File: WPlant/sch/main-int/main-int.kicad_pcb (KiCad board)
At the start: 2 copper layers, 135 x 85 mm, 139 parts, among them J1 PROG/JTAG, J10 Ext, J11 HSensor, J12 HSensor, J13 HSensor, J14 HSensor, J15 HSensor, J16 HSensor, J17 HSensor, J18 WaterLevel, J5 220V, J6 Conn_01x08_Pin, J8 eInk-Buttons, J9 Leak, M1 Motor_DC, Q1 FDS9926A, Q2 FDS9926A, Q3 FDS9926A, Q4 FDS9926A, U1 SIWG917Y121MGABAR, U10 SP485EEN-L/TR, U11 TXU0102QDCURQ1, U12 CD74HCT4051M96, U13 CD74HCT4051M96, U14 SN74LVC1G14DBV, U3 AP64352SP-13, U4 AP64352SP-13, U5 TC4427AEOA713, U6 AP2204R-5.0, U7 74HC594, U8 NC7S02P5, U9 INA180A2, X1 SIT1552AI-JE-DCC-32.768D

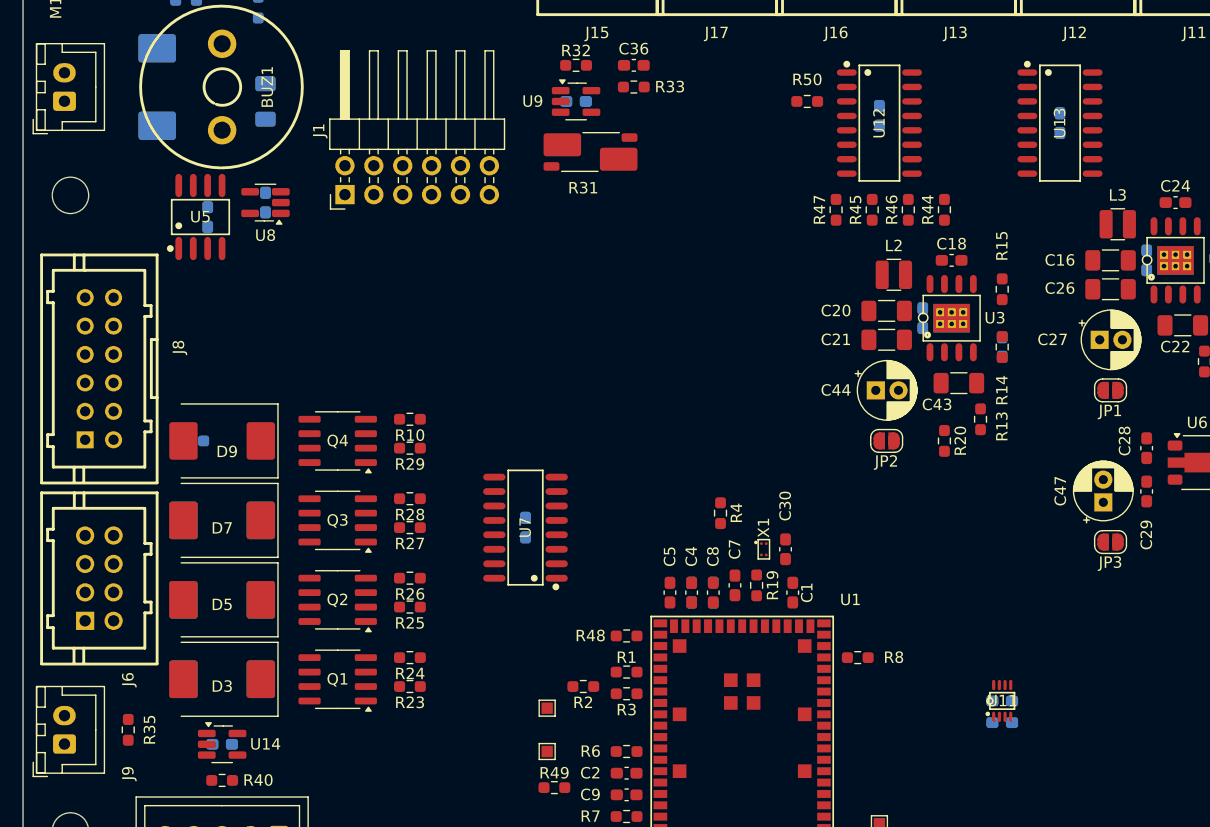
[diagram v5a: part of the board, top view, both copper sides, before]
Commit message: Started routing of MainInt
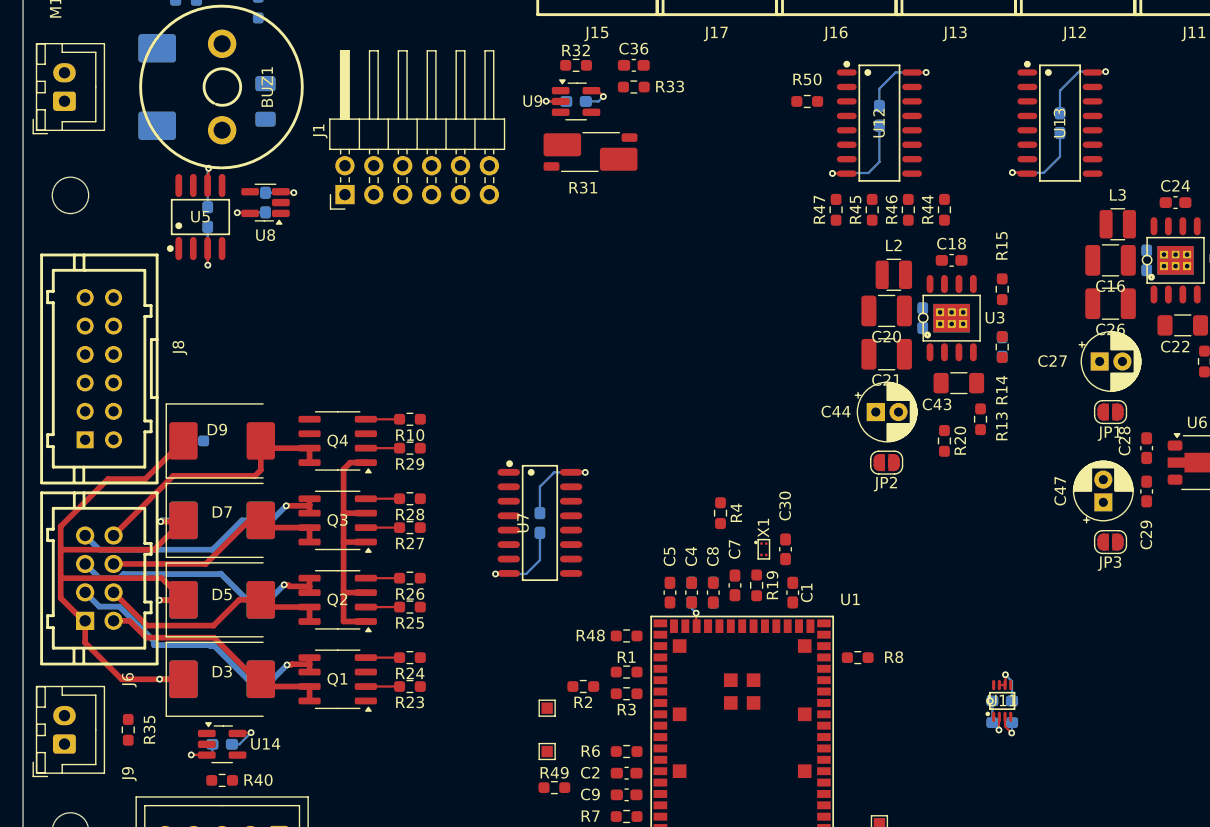
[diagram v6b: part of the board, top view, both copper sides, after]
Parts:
- C16, C20, C21, C26: footprint Capacitor_SMD:C_1206_3216Metric_Pad1.33x1.80mm_HandSolder -> Capacitor_SMD:C_1210_3225Metric_Pad1.33x2.70mm_HandSolder
- moved C44 1.91 mm to (161.0, 97.2)
- moved JP1 1.91 mm to (181.6, 97.2)
- moved JP2 1.91 mm to (161.9, 101.6)
- moved C27 1.90 mm to (180.7, 92.7)
- moved C34 1.33 mm to (131.4, 106.9), turned to -90 degrees
- moved U7 1.33 mm to (131.4, 106.9), turned to -90 degrees
- moved C21 1.27 mm to (161.9, 92.1)
- moved C26 1.27 mm to (181.6, 87.6)
- turned C40 to 90 degrees
- turned C41 to 90 degrees
- turned D3 to 0 degrees
- turned D4 to 0 degrees
- turned D5 to 0 degrees
- turned D6 to 0 degrees
- turned D7 to 0 degrees
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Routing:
- net +9V: track 0.00 -> 69.1 mm, vias 0 -> 3
- net GND: track 0.00 -> 68.2 mm, vias 0 -> 8
- net Net-(D4-A): track 0.00 -> 24.9 mm, vias 0 -> 1
- net Net-(D9-A): track 0.00 -> 23.7 mm
- net Net-(D6-A): track 0.00 -> 23.2 mm, vias 0 -> 1
- net Net-(D8-A): track 0.00 -> 23.1 mm, vias 0 -> 1
- net Net-(D5-A): track 0.00 -> 20.9 mm
- net +5V: track 0.00 -> 20.9 mm, vias 0 -> 4
- net Net-(D3-A): track 0.00 -> 20.9 mm
- net Net-(D7-A): track 0.00 -> 20.3 mm
- net +3.3V: track 0.00 -> 18.0 mm, vias 0 -> 4
- net VBUS: track 0.00 -> 5.02 mm, vias 0 -> 1
- net Net-(U12-A7): track 0.00 -> 3.33 mm, vias 0 -> 1
- net Net-(Q4B-G2): track 0.00 -> 2.96 mm
- net Net-(Q4A-G1): track 0.00 -> 2.96 mm
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
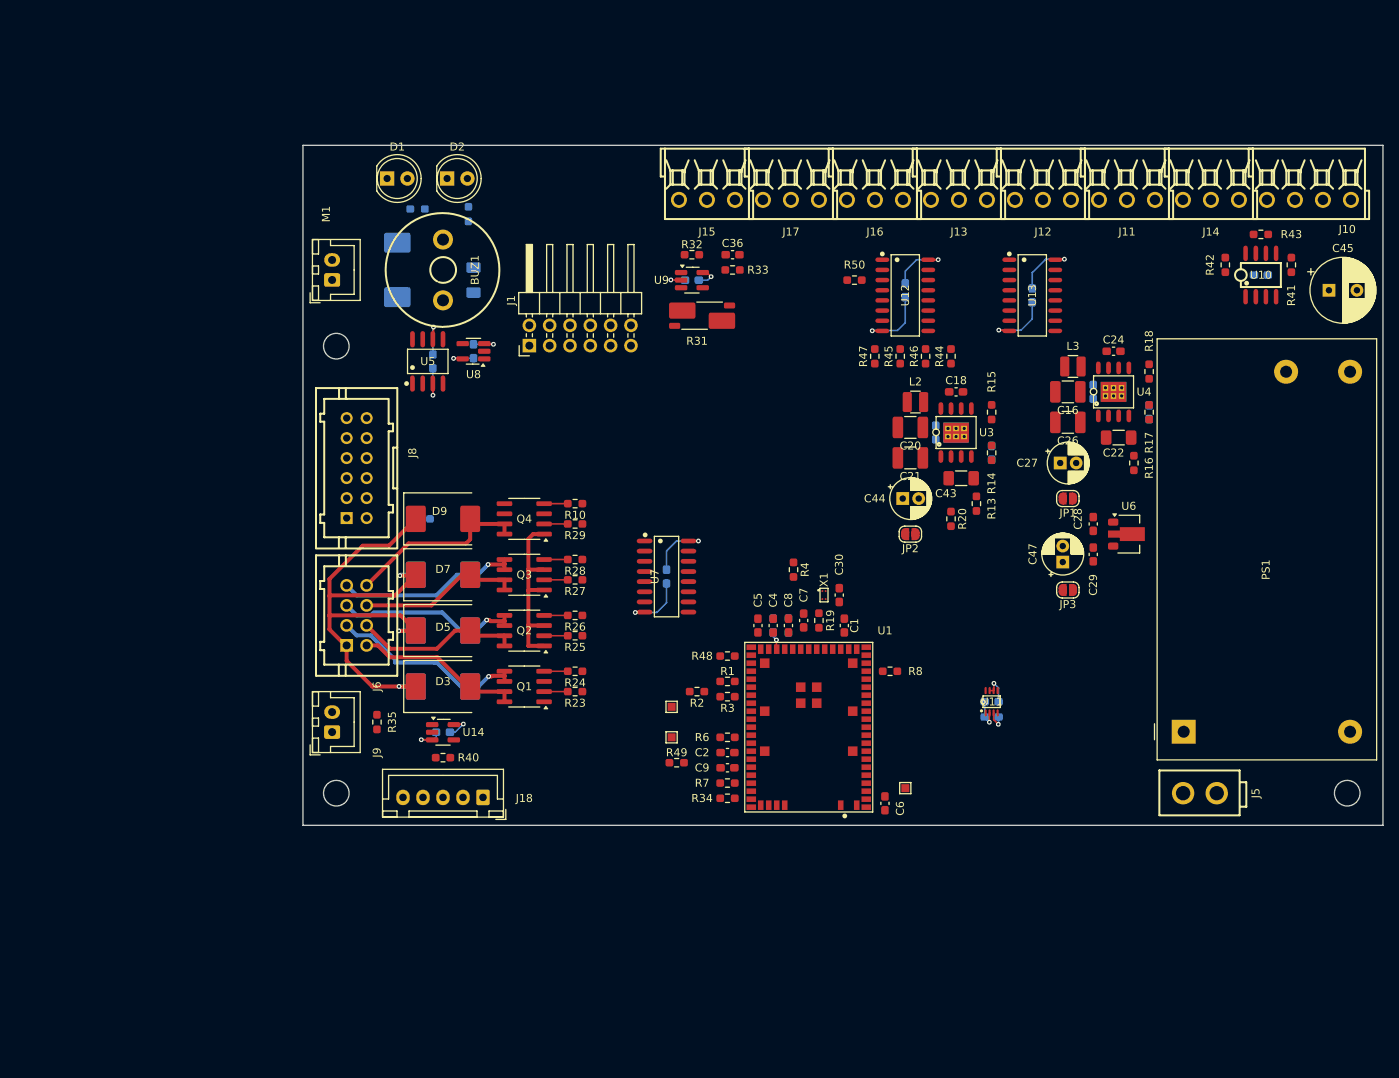
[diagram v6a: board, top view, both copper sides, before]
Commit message: Route of MainInt PCB almost done
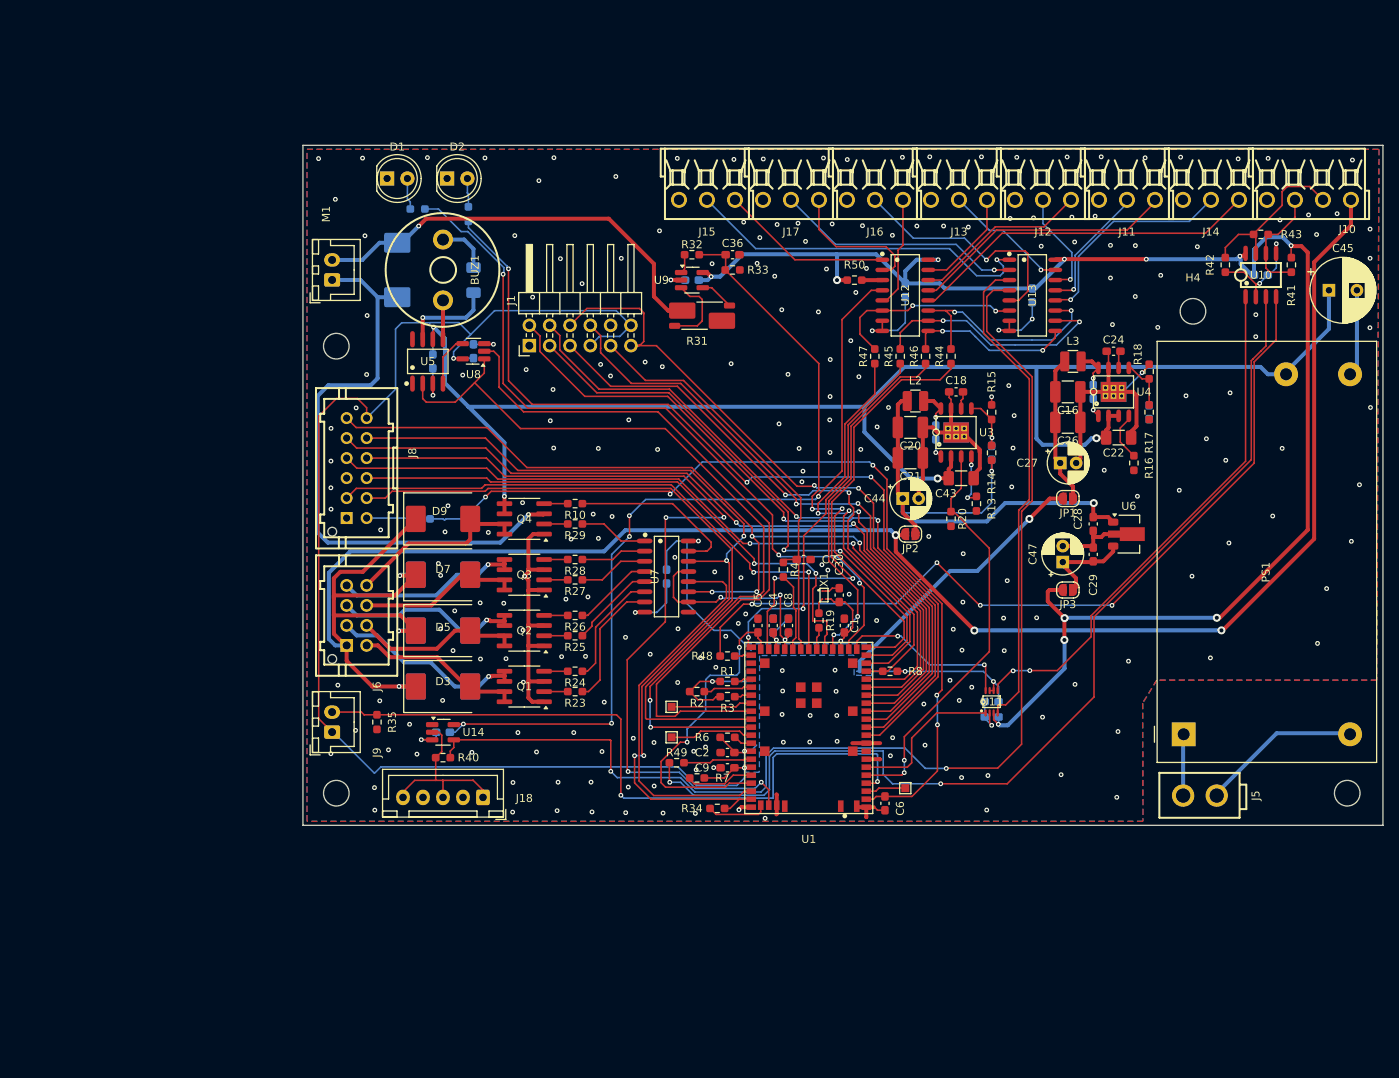
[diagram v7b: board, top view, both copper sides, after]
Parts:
- added H4: MountingHole, MountingHole:MountingHole_3.2mm_M3, F.Cu at (197.2, 73.8)
- J6: footprint easyeda2kicad:CONN-TH_8P-P2.50_XAD-8A -> locals:CONN-TH_8P-P2.50_XAD-8AS
- J8: footprint easyeda2kicad:CONN-TH_XAD-12A -> locals:CONN-TH_XAD-12AS
- U1: footprint easyeda2kicad:COMM-SMD_SIWG917Y110LGNBA -> locals:COMM-SMD_SIWG917Y110LGNBA
- moved C7 7.62 mm to (148.6, 104.8), turned to 180 degrees
- moved R7 3.86 mm to (135.3, 132.1), turned to 0 degrees
- moved R34 1.80 mm to (137.8, 135.9)
- moved R4 1.27 mm to (146.1, 106.0)
- moved L3 0.63 mm to (182.2, 80.0)
- moved PS1 0.31 mm to (196.1, 126.6)
- moved J5 0.30 mm to (198.1, 134.3)
- moved L2 0.13 mm to (162.6, 85.0)
- turned R9 to 0 degrees
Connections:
- R10 pad 1: Net-(U7-QH) -> Net-(U7-QA)
- R23 pad 1: Net-(U7-QA) -> Net-(U7-QH)
- R24 pad 1: Net-(U7-QB) -> Net-(U7-QG)
- R25 pad 1: Net-(U7-QC) -> Net-(U7-QF)
- R26 pad 1: Net-(U7-QD) -> Net-(U7-QE)
- R27 pad 1: Net-(U7-QE) -> Net-(U7-QD)
- R28 pad 1: Net-(U7-QF) -> Net-(U7-QC)
- R29 pad 1: Net-(U7-QG) -> Net-(U7-QB)
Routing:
- net +3.3V: track 18.0 -> 297.3 mm, vias 4 -> 10
- net +9V: track 69.1 -> 260.3 mm, vias 3 -> 6
- net VBUS: track 5.02 -> 190.8 mm, vias 1 -> 4
- net +5V: track 20.9 -> 199.8 mm, vias 4 -> 11
- net Net-(U13-A7): track 0.00 -> 147.2 mm, vias 0 -> 2
- net Net-(U10-DE): track 0.00 -> 127.8 mm, vias 0 -> 2
- net GND: track 68.2 -> 194.1 mm, vias 8 -> 253
- net /eInkCLK: track 0.00 -> 113.8 mm, vias 0 -> 4
- net /eInkData: track 0.00 -> 113.5 mm, vias 0 -> 4
- net Net-(U1-GPIO_55): track 0.00 -> 113.3 mm, vias 0 -> 3
- net Net-(U1-UULP_VBAT_GPIO_0): track 0.00 -> 111.5 mm, vias 0 -> 5
- net /~{eInkCS}: track 0.00 -> 110.0 mm, vias 0 -> 4
- net Net-(U10-DI): track 0.00 -> 105.2 mm, vias 0 -> 4
- net /BUZZ: track 0.00 -> 101.6 mm, vias 0 -> 2
- net Net-(U12-A7): track 3.33 -> 103.3 mm, vias 1 -> 5
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- added copper zone on B.Cu, net +3.3V
- added copper zone on B.Cu, net GND
- added copper zone on F.Cu, net GND

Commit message: Route of MainInt PCB done
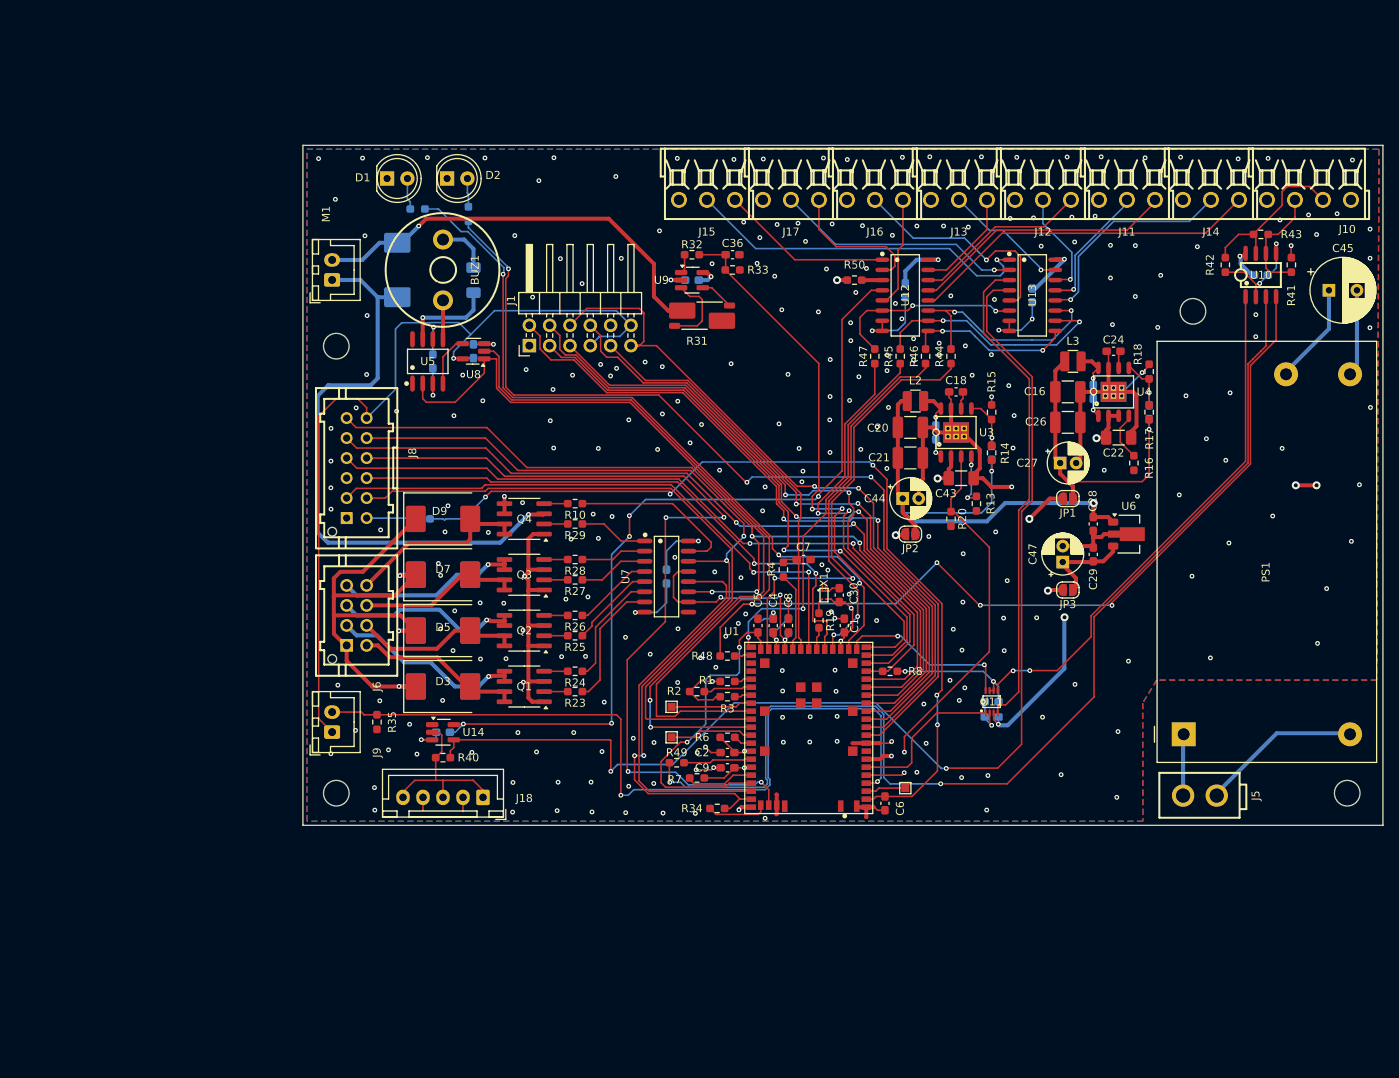
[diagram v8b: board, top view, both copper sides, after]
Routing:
- net +9V: track 260.3 -> 347.0 mm
- net +3.3V: track 297.3 -> 227.8 mm, vias 10 -> 11
- net GND: track 194.1 -> 223.1 mm, vias 253 -> 286
- net Net-(JP1-A): track 18.5 -> 37.3 mm, vias 0 -> 1
- net Net-(J9-Pin_2): track 88.4 -> 98.9 mm
- net Net-(U10-DE): track 127.8 -> 137.6 mm
- net +5V: track 199.8 -> 203.4 mm, vias 11 -> 9
- net /Humidity/F6: track 30.3 -> 28.7 mm
- net Net-(U4-FB): track 6.36 -> 7.95 mm, vias 0 -> 1
- net /BUZZ: track 101.6 -> 103.1 mm
- net Net-(U1-GPIO_52): track 94.4 -> 93.0 mm
- net PROG-TX: track 71.0 -> 72.3 mm
- net JTAG-TDI: track 82.6 -> 83.8 mm
- net JTAG-TMS: track 89.3 -> 90.5 mm
- net /~{BUZZ-EN}: track 90.2 -> 89.1 mm
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- added copper zone on In1.Cu, net +3.3V
- added copper zone on In1.Cu, net GND
- added copper zone on In2.Cu, net GND
- removed copper zone on B.Cu, net +3.3V
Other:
- copper layers 2 -> 4
